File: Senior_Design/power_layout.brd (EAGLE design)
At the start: 105.8 x 35 mm, 42 parts, among them IC1 MIC29302WU, J1[SIMCARD] 78646-3001, J2 292303-1, J3[GROVE] 640456-4, J4[GROVE] 640456-4, T1 2N706, T2 2N706, U1 SIM7000E, U2 TUSB2046BIRHBR, U3 PCA9306DQER

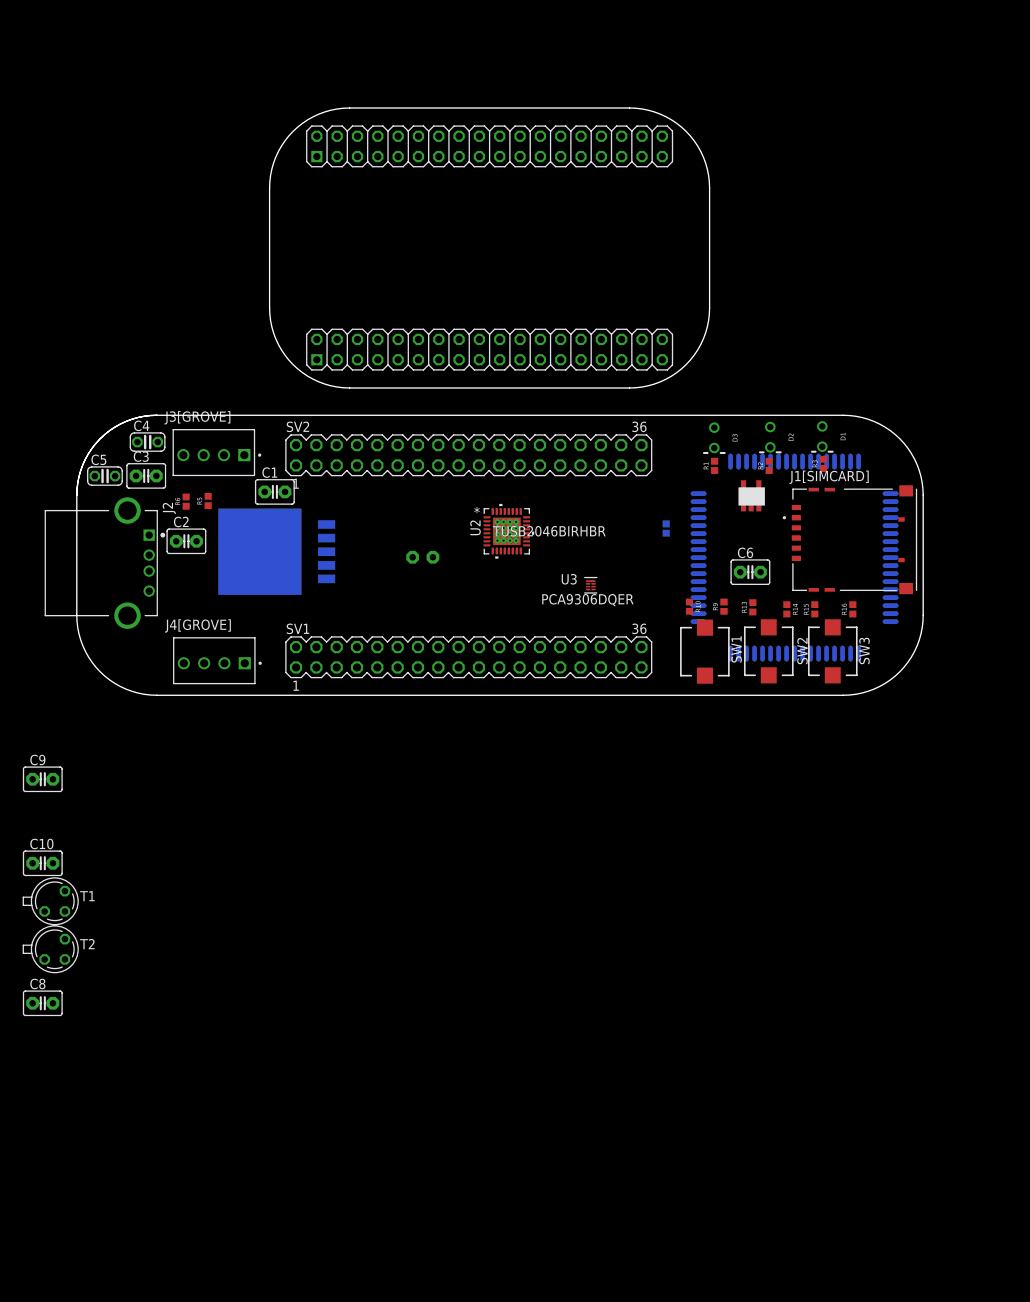
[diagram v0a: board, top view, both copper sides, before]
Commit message: Add files via upload
Schematic Reflects all changes as discussed in Sep 1st HW meeting.  Layout will begin tomorrow.
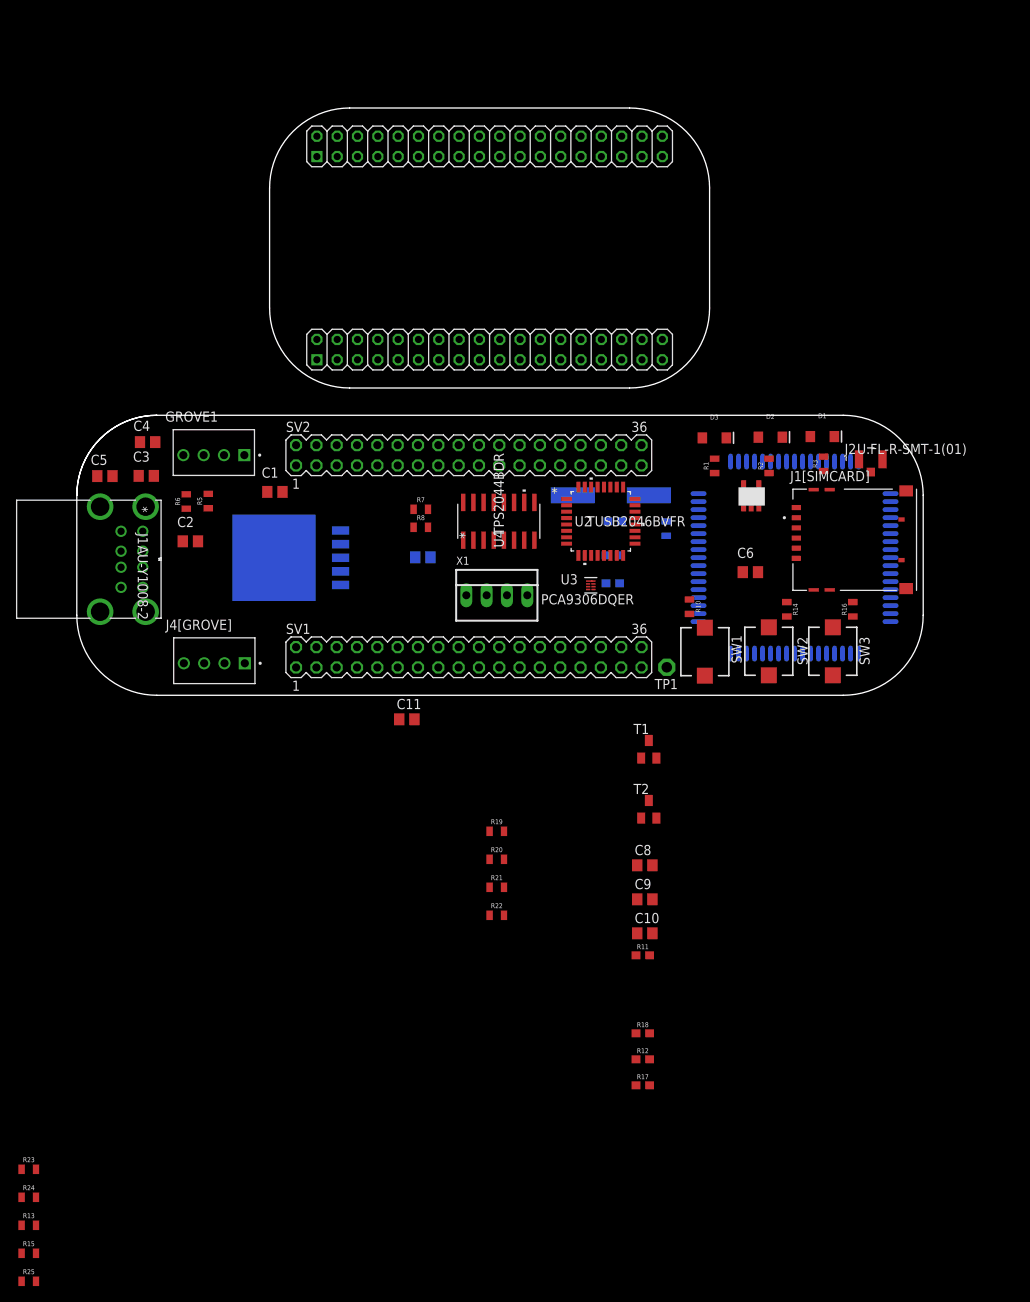
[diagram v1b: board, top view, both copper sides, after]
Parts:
- added C11: (no value), rcl:C0805
- added C12, C13: 27pF, rcl:C0603
- added CR1: 9C-6.000MAAJ-T, Personal:CRYSTAL_TXC_9C_TXC
- added J1: AU-Y1008-2, Personal:CONN_AU-Y1008-2_ASM
- added R11, R18: 47k, SparkFun-Resistors:0603
- added R12, R17: 4.7k, SparkFun-Resistors:0603
- added R19, R20, R7, R8: 27, SparkFun-Resistors:0805
- added R21, R22: (no value), SparkFun-Resistors:0805
- added R23, R24: 15k, SparkFun-Resistors:0805
- added R25: 1.5k, SparkFun-Resistors:0805
- added TP1: TPPAD1-13, testpad:P1-13
- added U4: TPS2044BDR, Personal:D16_TEX
- added X1: 22-23-2041, con-molex:22-23-2041
- C1: value 1uF -> (none); device capacitor-wima:C2.5-3 -> rcl:C0805
- C10, C2, C6, C7, C8, C9: device capacitor-wima:C2.5-3 -> rcl:C0805
- C3: value 0.1 uF -> (none); device capacitor-wima:C2.5-3 -> rcl:C0805
- C4: value 100 uF -> (none); device rcl:C025-024X044 -> rcl:C0805
- C5: value 330 uF -> (none); device rcl:C025-024X044 -> rcl:C0805
- D1: value (none) -> RED; device SparkFun-LED:LED_3MM-NS -> SparkFun-LED:LED-1206
- D2: value (none) -> GREEN; device SparkFun-LED:LED_3MM-NS -> SparkFun-LED:LED-1206
- D3: value (none) -> BLUE; device SparkFun-LED:LED_3MM-NS -> SparkFun-LED:LED-1206
- J2: value 292303-1 -> U.FL-R-SMT-1(01); device 292303-1:TE_292303-1 -> Personal:CONN_-SMT-1(01)
- R1, R10, R14, R16, R2, R3: device SparkFun-Resistors:0402 -> SparkFun-Resistors:0805
- R13, R15: value (none) -> 15k; device SparkFun-Resistors:0402 -> SparkFun-Resistors:0805
- R4: value 47k -> (none); device SparkFun-Resistors:0402 -> SparkFun-Resistors:0805
- R5: value 100k -> (none); device SparkFun-Resistors:0402 -> SparkFun-Resistors:0805
- R6: value 470 -> (none); device SparkFun-Resistors:0402 -> SparkFun-Resistors:0805
- R9: value (none) -> 1.5k; device SparkFun-Resistors:0402 -> SparkFun-Resistors:0603
- T1, T2: value 2N706 -> BCX70SMD; device transistor:TO18 -> transistor:SOT23
- U2: value TUSB2046BIRHBR -> TUSB2046BVFR; device TUSB2046B:RHB32_3P45X3P45 -> Personal:VF32_TEX
- moved R15 127.0 mm to (-6.00, -69.8), turned to 0 degrees
- moved R13 119.0 mm to (-6.00, -66.2), turned to 0 degrees
- moved J2 90.7 mm to (99.2, 29.5), turned to 0 degrees
- moved C8 77.2 mm to (71.0, -21.2)
- moved C9 76.7 mm to (71.0, -25.5)
- moved T1 76.6 mm to (71.5, -6.75)
- moved T2 76.3 mm to (71.5, -14.2)
- moved C10 75.8 mm to (71.0, -29.8)
- moved R9 17.3 mm to (67.2, 21.8), flipped to the bottom, turned to 0 degrees
- moved U2 11.8 mm to (65.5, 21.8)
- moved IC1 1.90 mm to (27.2, 17.2)
- moved C2 0.50 mm to (14.2, 19.2)
- turned D1 to 0 degrees
- turned D2 to 0 degrees
- turned D3 to 0 degrees
- renumbered J3[GROVE] to GROVE1
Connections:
- removed net +3V3: C9.1, U3.7, U3.8
- removed net GND_2: U2.7
- removed net GPIO_1: R3.2
- removed net GPIO_3: R1.2
- removed net N$11: R9.1, SW1.P$2
- removed net N$15: R15.1, SW3.P$2
- removed net TP01: U1.6
- removed net UART_RXD: U1.10, U3.5
- removed net UART_TXD: U1.9, U3.6
- removed net VCC: U2.25
- removed net VCC_2: U2.3
- removed net WIFI_D+: J2.3
- removed net WIFI_D-: J2.2
- new net 1.8V: C9.1, U1.15, U3.2
- new net 3.3V: C10.1, R25.2, SV1.14, U2.25, U2.26, U2.3, U3.7, U3.8, X1.1
- new net ANT: J2.2, U1.60
- new net DM0: R8.1, SV1.9
- new net DP0: R7.1, SV1.11
- new net I2C1_SCL: C2.2, GROVE1.1, SV2.9
- new net I2C1_SDA: GROVE1.2, SV2.11
- new net I2C2_SCL: C7.2, J4[GROVE].1
- new net I2C2_SDA: J4[GROVE].2
- new net LED1: R3.2, SV2.6
- new net LED2: R2.2, SV2.8
- new net LED3: R1.2, SV2.10
- new net N$13: U3.6, X1.2
- new net N$16: U3.5, X1.3
- new net N$17: R11.1, R12.2, T2.1
- new net N$18: R17.1, R18.2, T1.1
- new net N$19: R19.2, U2.15
- new net N$20: R20.2, U2.16
- new net N$21: J4[GROVE].3
- new net N$22: R21.1, U2.20
- new net N$23: R22.1, U2.19
- new net N$24: GROVE1.3
- new net N$25: U2.24
- new net N$26: U2.23
- new net N$27: U1.10, U3.3
- new net N$28: U1.9, U3.4
- new net OUT1: U4.15
- new net OUT2: J1.1, U4.14
- new net OUT3: J1.5, U4.11
- new net OUT4: U4.10
- new net OVRCUR1: U2.10, U4.16
- new net OVRCUR2: U2.14, U4.13
- new net OVRCUR3: U2.18, U4.12
- new net OVRCUR4: U2.22, U4.9
- new net PB2: R14.2, SV2.17, SW2.P$1
- new net PB3: R16.2, SV2.19, SW3.P$1
- new net PWRKEY: C8.1, SV2.3, T1.3, U1.1
- new net PWRON1: U2.9, U4.3
- new net PWRON2: U2.13, U4.4
- new net PWRON3: U2.17, U4.7
- new net PWRON4: U2.21, U4.8
- new net USB1_D+: J1.3, R20.1, R24.2
- new net USB1_D-: J1.2, R19.1, R23.2
- new net USB2_D+: J1.7, R13.2, R21.2
- new net USB2_D-: J1.6, R15.2, R22.2
- new net XTAL1: C12.1, CR1.1, U2.30
- new net XTAL2: R9.2, U2.29
- net +5V: now also C11.1, SW1.P$2, SW2.P$2, SW3.P$2, U4.2, U4.6; no longer C2.2, C7.2, GROVE1.1, GROVE1.2, GROVE1.3, J2.1, J4[GROVE].1, J4[GROVE].2, J4[GROVE].3, R13.2, R15.2, R9.2
- net 0: now also C11.2, C12.2, C13.2, R13.1, R15.1, R23.1, R24.1, U2.6, U2.7, U2.8; no longer C1.2, C10.1, C2.1, C3.2, C4.2, C5.2, C6.2, C7.1, C8.1, C9.2, D1.K, D2.K, D3.K, GROVE1.4, IC1.3, J1[SIMCARD].C5, J1[SIMCARD].G1, J1[SIMCARD].G2, J1[SIMCARD].G3, J1[SIMCARD].G4, J1[SIMCARD].G5, J1[SIMCARD].G6, J2.4, J4[GROVE].4, R10.1, R14.1, R16.1, R4.1, R6.1, T1.1, T2.1, U$1.P$2, U1.17, U1.18, U1.2, U1.29, U1.39, U1.45, U1.46, U1.54, U1.58, U1.59, U1.61, U1.62, U1.63, U1.64, U1.65, U3.1
- net GND: now also C1.2, C10.2, C2.1, C3.2, C4.2, C5.2, C6.2, C7.1, C8.2, C9.2, D1.C, D2.C, D3.C, GROVE1.4, IC1.3, J1.4, J1.8, J1[SIMCARD].C5, J1[SIMCARD].G1, J1[SIMCARD].G2, J1[SIMCARD].G3, J1[SIMCARD].G4, J1[SIMCARD].G5, J1[SIMCARD].G6, J2.1, J2.3, J4[GROVE].4, R10.1, R11.2, R14.1, R16.1, R18.1, R4.1, R6.1, SV1.15, SV2.15, T1.2, T2.2, U$1.P$2, U1.17, U1.18, U1.2, U1.29, U1.39, U1.45, U1.46, U1.54, U1.58, U1.59, U1.61, U1.62, U1.63, U1.64, U1.65, U2.27, U2.31, U3.1, U4.1, U4.5, X1.4
- net MODEM_D+: now also U2.12
- net MODEM_D-: now also U2.11
- net N$10: now also R25.1, R7.2, U2.1; no longer C10.2, T1.3, U1.1
- net N$12: now also R8.2, U2.2; no longer C8.2, U3.2
- net N$14: now also C13.1, CR1.2, R9.1; no longer R13.1, SW2.P$2
- net N$9: now also TP1.TP, U1.6; no longer R2.2
- net NRESET: now also SV2.4; no longer R14.2, R16.2, SW2.P$1, SW3.P$1
- net PWR: now also R17.2; no longer T1.2
- net SLEEP: now also R12.1; no longer T2.2
- net VDD_EXT: no longer U1.15

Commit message: Add files via upload
Another push inbound
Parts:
- added C14, C15: 27pF, rcl:C0603
- added D4: Yellow, SparkFun-LED:LED-0603
- added R26, R27: 0, SparkFun-Resistors:0603
- added R28: 330, SparkFun-Resistors:0603
- added TP2: TPTP16R, testpad:TP16R
- R1, R2, R3: value (none) -> 330
- TP1: value TPPAD1-13 -> TPTP10R; device testpad:P1-13 -> testpad:TP10R
- X1: value 22-23-2041 -> 332-04; device con-molex:22-23-2041 -> con-garry:332-04
- moved R13 65.9 mm to (35.4, -14.9)
- moved R15 65.9 mm to (35.4, -18.4)
- moved R23 65.9 mm to (35.4, -7.94)
- moved R24 65.9 mm to (35.4, -11.4)
- moved R25 65.9 mm to (35.4, -21.9)
- moved R22 43.3 mm to (52.2, 15.8)
- moved R21 40.5 mm to (61.3, 15.5)
- moved R20 36.5 mm to (58.3, 15.6)
- moved R19 32.8 mm to (55.3, 15.6)
- moved X1 24.1 mm to (75.2, 4.50)
- moved C11 12.6 mm to (44.4, 9.19)
- moved C6 12.1 mm to (90.7, 25.7)
- moved BRD1 11.5 mm to (23.9, 49.9)
- moved U3 11.0 mm to (74.2, 8.92)
- moved C13 10.2 mm to (72.3, 22.6)
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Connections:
- net VBAT renamed MODEM_POWER
- removed net 0: C11.2, C12.2, C13.2, R13.1, R15.1, R23.1, R24.1, U2.6, U2.7, U2.8
- removed net ANT: J2.2, U1.60
- new net N$11: C14.1, R26.1, R27.2
- new net N$15: TP2.TP, U1.53
- new net N$29: R28.2, U1.52
- new net N$30: D4.A, R28.1
- new net PRE_ANT: C15.1, R26.2, U1.60
- new net RF_ANT: J2.2, R27.1
- net GND: now also C11.2, C12.2, C13.2, C14.2, C15.2, D4.C, R13.1, R15.1, R23.1, R24.1, U2.6, U2.7, U2.8
- net NRESET: no longer SV2.4
- net SLEEP: now also SV2.2
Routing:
- net GND: track 0.00 -> 138.7 mm, vias 0 -> 10
- net MODEM_POWER: track 0.00 -> 72.9 mm, vias 0 -> 2
- net PB3: track 0.00 -> 66.1 mm, vias 0 -> 3
- net PB2: track 0.00 -> 63.9 mm, vias 0 -> 3
- net LED1: track 0.00 -> 63.3 mm, vias 0 -> 1
- net LED2: track 0.00 -> 50.7 mm, vias 0 -> 1
- net LED3: track 0.00 -> 37.3 mm, vias 0 -> 1
- net +5V: track 0.00 -> 32.6 mm, vias 0 -> 1
- net N$6: track 0.00 -> 25.3 mm, vias 0 -> 1
- net N$1: track 0.00 -> 23.1 mm, vias 0 -> 1
- net N$2: track 0.00 -> 20.9 mm, vias 0 -> 1
- net N$4: track 0.00 -> 16.6 mm, vias 0 -> 3
- net PRE_ANT: track 0.00 -> 13.1 mm, vias 0 -> 1
- net NRESET: track 0.00 -> 7.22 mm, vias 0 -> 1
- net N$11: track 0.00 -> 4.50 mm
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
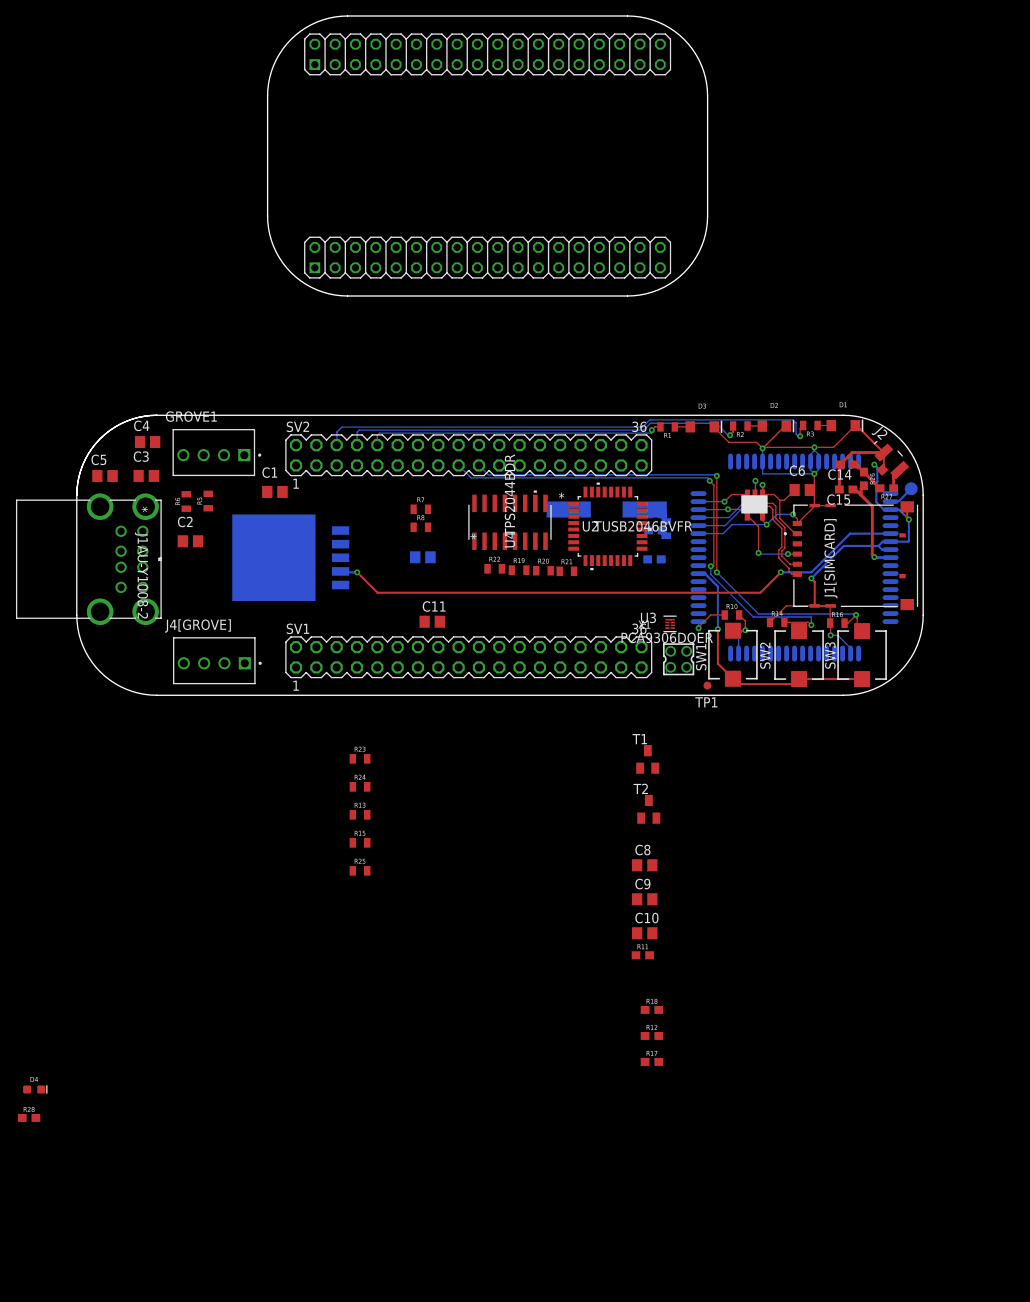
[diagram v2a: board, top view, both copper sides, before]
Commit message: Add files via upload
Nightly progress pre-CDR
-Still finishing Layout
~2 hours of layout left until first draft complete
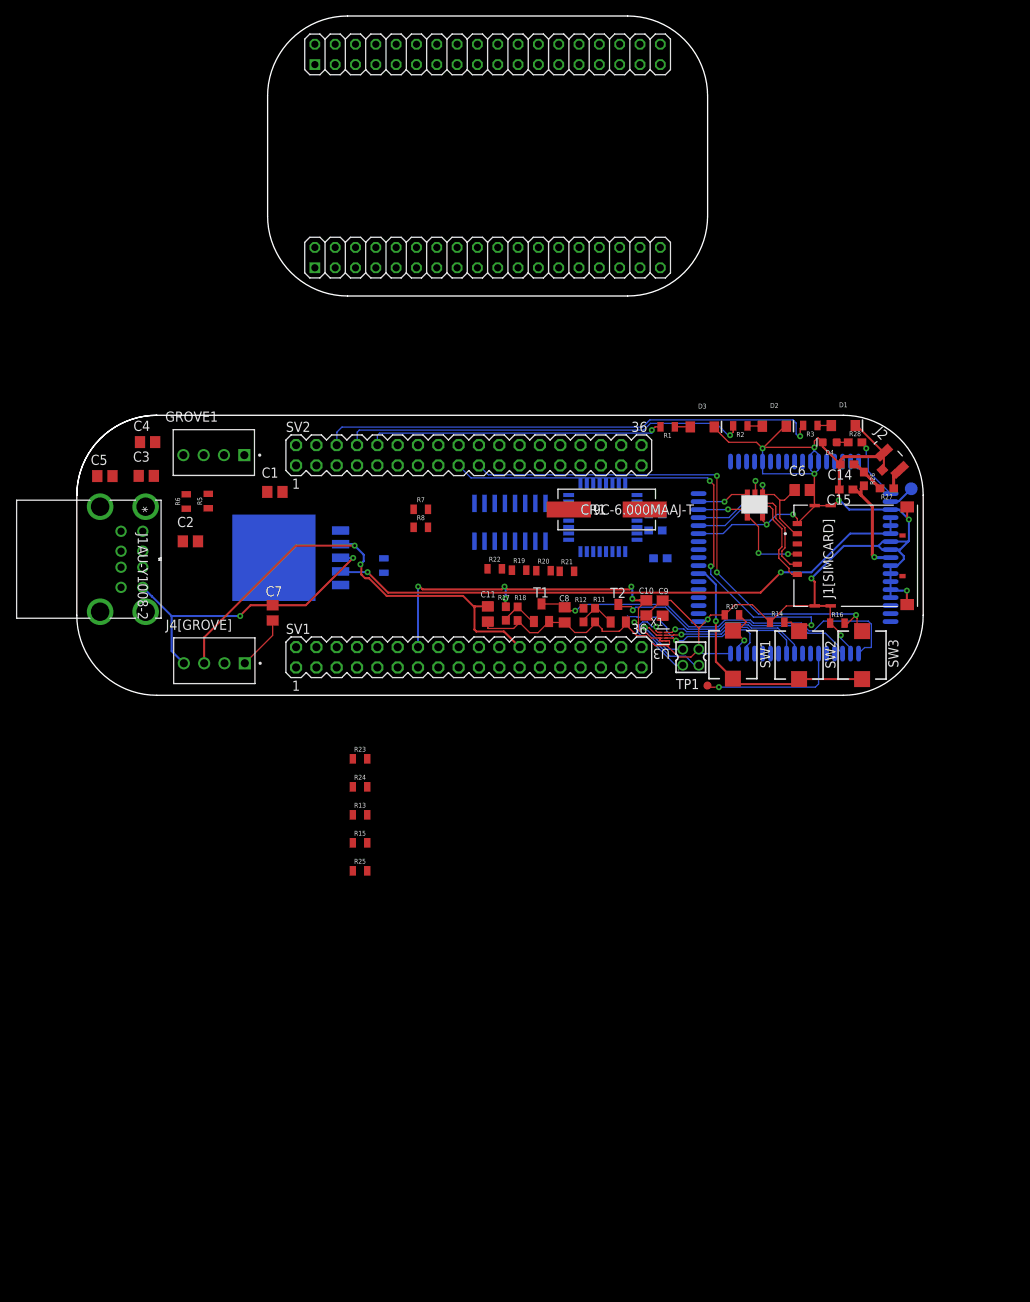
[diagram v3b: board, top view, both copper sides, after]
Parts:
- moved R28 133.4 mm to (97.3, 31.6)
- moved D4 128.2 mm to (94.1, 31.6), turned to 180 degrees
- moved R17 59.0 mm to (53.6, 10.2), turned to 90 degrees
- moved R12 53.3 mm to (63.3, 10.0), turned to 270 degrees
- moved R18 52.3 mm to (55.1, 10.2), turned to 90 degrees
- moved R11 42.9 mm to (64.8, 10.0), turned to 270 degrees
- moved C10 40.7 mm to (71.2, 10.9), turned to 270 degrees
- moved C9 36.5 mm to (73.2, 10.9), turned to 90 degrees
- moved R4 35.6 mm to (38.4, 16.2), turned to 270 degrees
- moved C8 32.9 mm to (61.0, 10.1), turned to 270 degrees
- moved T2 24.8 mm to (67.7, 10.3)
- moved T1 22.6 mm to (58.1, 10.3)
- moved C7 20.0 mm to (24.5, 10.3), flipped to the top, turned to 270 degrees
- moved C11 7.02 mm to (51.4, 10.2), turned to 270 degrees
- moved U3 1.81 mm to (73.3, 7.33), turned to 180 degrees
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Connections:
- removed net N$21: J4[GROVE].3
- removed net N$24: GROVE1.3
- removed net PWR: R17.2
- net +5V: now also GROVE1.3, J4[GROVE].3, SV1.24
- net 3.3V: now also R17.2
- net I2C2_SCL: now also SV1.28
- net I2C2_SDA: now also SV1.26
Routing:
- net GND: track 138.7 -> 252.9 mm, vias 10 -> 13
- net +5V: track 32.6 -> 92.5 mm, vias 1 -> 3
- net 3.3V: track 0.00 -> 58.5 mm, vias 0 -> 6
- net PWRKEY: track 0.00 -> 49.5 mm, vias 0 -> 1
- net VDD_EXT: track 0.00 -> 32.0 mm, vias 0 -> 1
- net 1.8V: track 0.00 -> 21.7 mm, vias 0 -> 1
- net N$28: track 0.00 -> 18.9 mm, vias 0 -> 1
- net N$9: track 0.00 -> 17.9 mm, vias 0 -> 1
- net N$27: track 0.00 -> 17.8 mm, vias 0 -> 1
- net N$16: track 0.00 -> 13.6 mm, vias 0 -> 1
- net N$13: track 0.00 -> 8.24 mm, vias 0 -> 1
- net N$29: track 0.00 -> 7.90 mm, vias 0 -> 1
- net I2C2_SCL: track 0.00 -> 6.80 mm
- net N$18: track 0.00 -> 5.08 mm
- net N$17: track 0.00 -> 4.96 mm
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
